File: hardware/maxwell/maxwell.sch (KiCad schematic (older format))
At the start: 33 parts, among them J1 Canbus 1, J10 SPI2_B, J11 BACKUP, J12 UART4, J13 UART5, J14 I2C1, J16 ESP_BM, J17 ESP_PROG, J19 Interconnect (Power), J2 SPI2_C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

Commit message: Updating PWR board to v1.7; adds:
* Fix for footprint of AP9101C (I have the five-pin package; not six)
* Grounding VM on the AP9101C to BAT- to disable current protection;
  I'm using the TPS2113A for current protection, so this feature isn't
  needed.
* Adds I2C-addressable INA219AID current sensor IC.
* Adds I2C-addressable PCF8593 counter for speed measurement.
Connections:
- net labels removed: SPEED
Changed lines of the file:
@@
 Text GLabel 5350 3450 0    60   BiDi ~ 0
 I2C1_SDA
-Text GLabel 5350 3350 0    60   Input ~ 0
-SPEED
-Text GLabel 5350 4500 0    60   Output ~ 0
-SPEED
 Text GLabel 5850 4600 2    60   BiDi ~ 0
 I2C1_SCL

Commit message: Revision 1.9a
* Separates PCB into three boards (from two); adding a new
  'Rectifier' board mounted directly to the 'Power' board via a
  board-to-board connector.
* Switches to active rectification.
* Provide 5V directly to the battery; drop VCC voltage to
  4.3V via a diode drop.
* Adds new WAKE-controlled power switch to reduce quiescent
  current to, essentially, nil, and remove the need
  carefully managing sleep states of various devices.
* Adds 220uF capacitor to 3V3 output on 'Main' PCB.
* Control power to SPI/I2C connector via a new uC-controlled MOSFET.
* Adds clock chip to main uC board for permanent timekeeping and
  alarm-based wakeup.
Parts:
- removed BZ1: Buzzer, coddingtonbear:12mm_buzzer, symbol maxwell-rescue:Buzzer-RESCUE-maxwell
- removed J13: UART5, coddingtonbear:JST_XH_B04B-XH-A_04x2.50mm_Straight_LargePads, symbol maxwell-rescue:Conn_01x04-conn
- removed J14: I2C1, coddingtonbear:JST_XH_B04B-XH-A_04x2.50mm_Straight_LargePads, symbol maxwell-rescue:Conn_01x04-conn
- removed J19: Interconnect (Power), coddingtonbear:IDC-Header_2x08_P2.54mm_Vertical_Largepads, symbol Connector_Generic:Conn_02x08_Odd_Even
- removed Q1: BSS138, coddingtonbear:SOT-23_LargePads, symbol maxwell-rescue:BSS138-RESCUE-maxwell
- removed R4: >35, coddingtonbear:0805_Milling, symbol maxwell-rescue:R-RESCUE-maxwell
- added C30: 0.1u, coddingtonbear:0805_Milling, symbol maxwell-rescue:C-RESCUE-maxwell
- added C31: 220u, coddingtonbear:CP_Tantalum_Case-C_EIA-6032-28_Milling, symbol Device:CP
- added C8, C9: 22p, coddingtonbear:0805_Milling, symbol maxwell-rescue:C-RESCUE-maxwell
- added D2: MBR1020VL, coddingtonbear:D_SOD-123_LargePads, symbol Device:D_Schottky
- added J15: I2C1, coddingtonbear:JST_XH_B04B-XH-A_04x2.50mm_Straight_LargePads, symbol maxwell-rescue:Conn_01x04-conn
- added Q1, Q2: DMG2302UK, coddingtonbear:SOT-23_LargePads, symbol Device:Q_NMOS_GSD
- added R32, R34, R35: 10k, coddingtonbear:0805_Milling, symbol maxwell-rescue:R-RESCUE-maxwell
- added SW1: SW_Push, coddingtonbear:SMD_MINI_BLACK_TACTILE_SWITCH, symbol Switch:SW_Push
- added U9: MCP79411-I/SN, coddingtonbear:SOIC-8_3.9x4.9mm_P1.27mm_LargePads, symbol Timer:MCP7940N-xSN
- added Y1: 32.768k, Crystal:Crystal_SMD_SeikoEpson_MC306-4Pin_8.0x3.2mm_HandSoldering, symbol maxwell-rescue:Crystal_GND23_Small-device
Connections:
- net labels added: +3V3_B, ENABLE_AUX, ENABLE_LEDS, GNDAUX, GND_B, I2C1_SCL_B, I2C1_SDA_B, VCC_B, WAKE_B, WAKE_B_SIG
- net labels removed: +3V3, BUZZER, CAN_DISABLE, GND, GNDPWR, I2C1_SCL, I2C1_SDA, POWER_ON, UART5_RX, UART5_TX, VCC
- wire segments 131 -> 168
- no-connect marks 26 -> 28
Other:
- moved on the sheet: C4, C5, J1, J10, J11, J12, J2, J20, J3, J5, R1, R31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

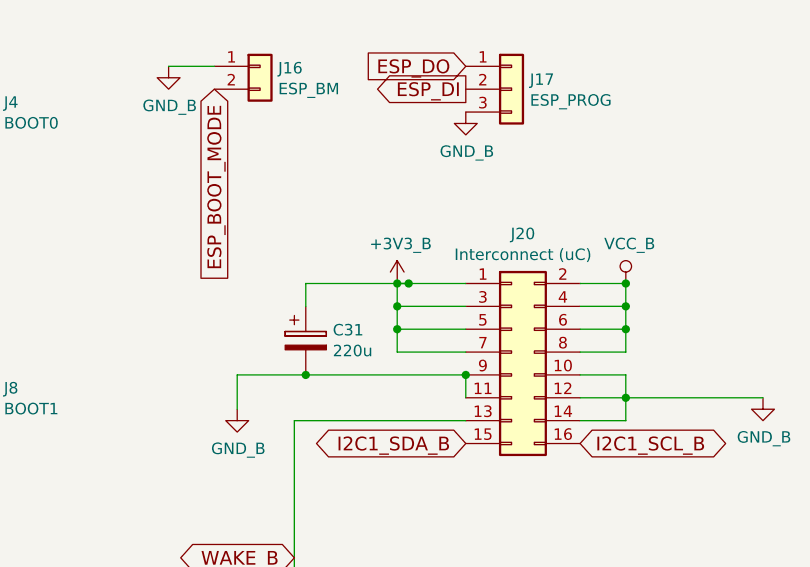
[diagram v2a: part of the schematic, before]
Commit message: Missing connection from diode controller to VDYN+; bodged.
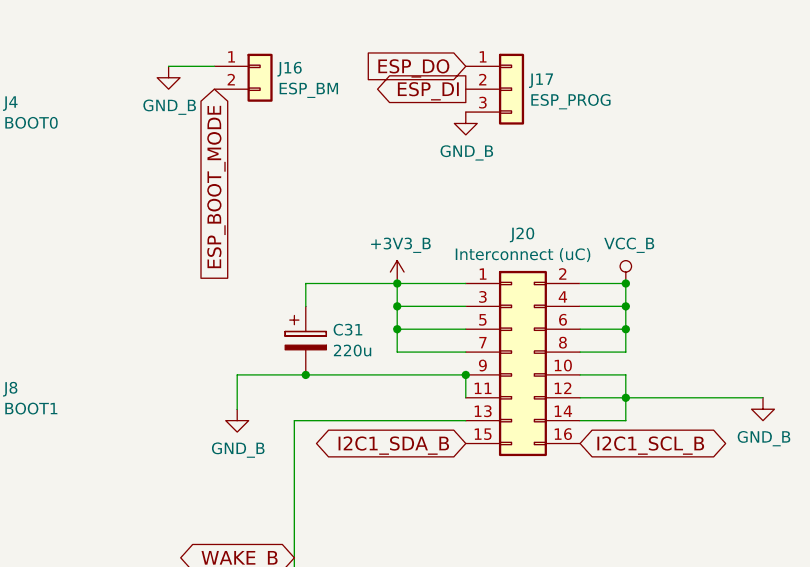
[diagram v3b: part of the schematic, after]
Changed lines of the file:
@@
 Wire Wire Line
 	4650 1900 5050 1900
-Connection ~ 5100 1900
-Wire Wire Line
-	5100 1900 5050 1900
 Wire Wire Line
 	4350 6150 5300 6150
-Wire Wire Line
-	5050 1900 5350 1900
 Connection ~ 5300 6150
 Wire Wire Line
 	5300 6150 5300 6400
+Wire Wire Line
+	5050 1900 5350 1900
 $EndSCHEMATC

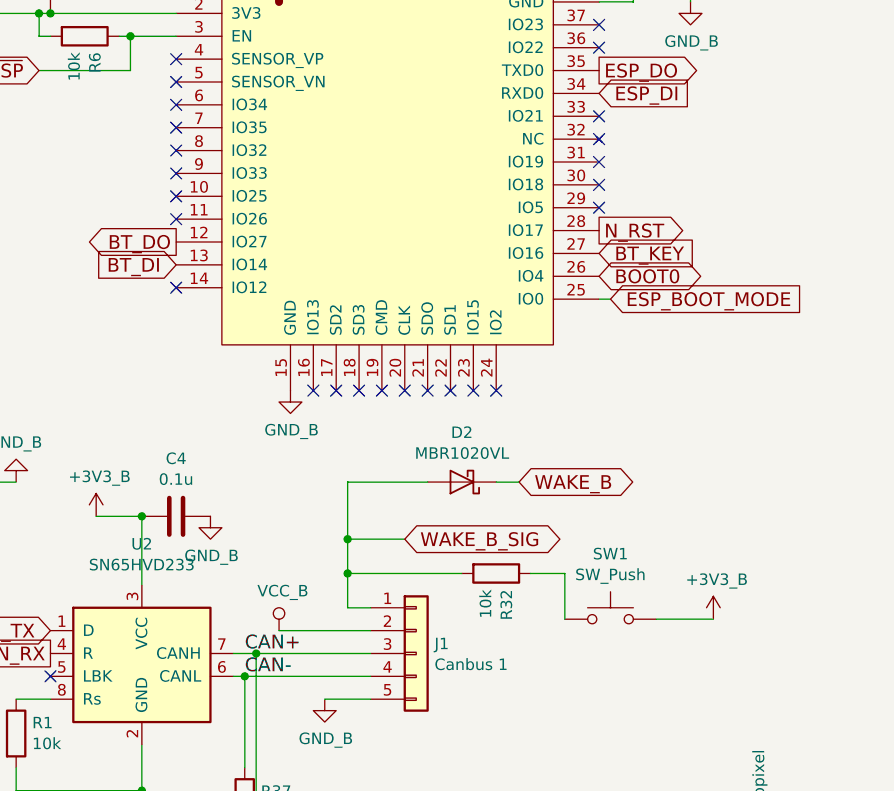
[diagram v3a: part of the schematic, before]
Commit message: Fixing errata:
* Connecting ESP32 to WAKE to ensure that the ESP32 can keep
  the power on while doing things like flashing the uC.
* Pull power button high to VCC via a diode instead of
  3V3 which is the very thing the power button will be
  turning on.
* Updating sense resistor to 100mOhm instead of 20mOhm.
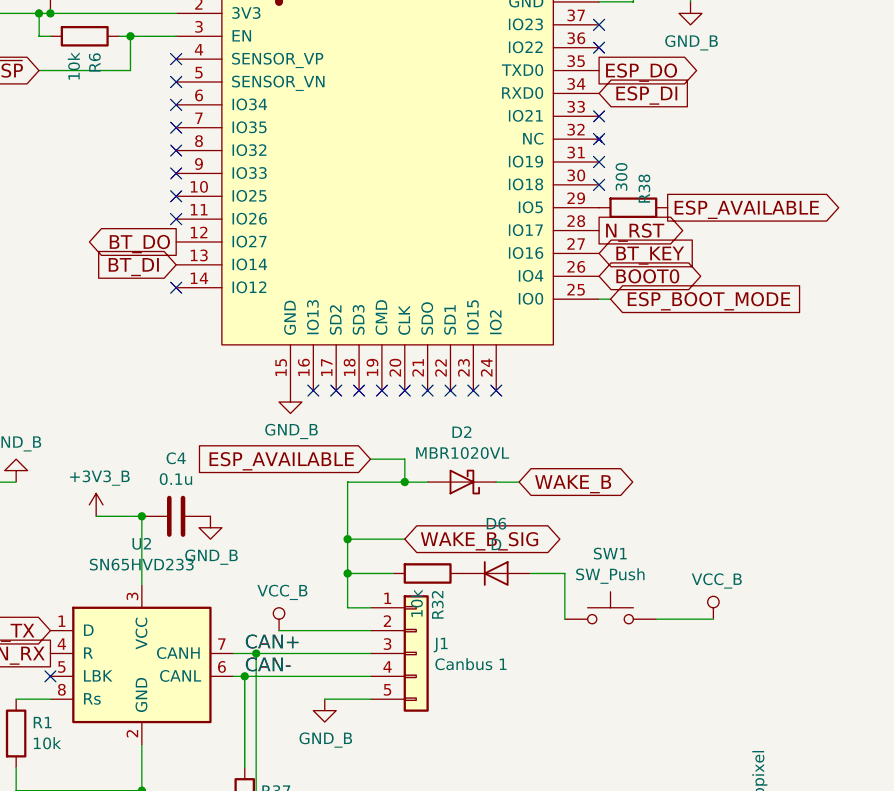
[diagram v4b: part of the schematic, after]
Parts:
- added D6: D, Diode_SMD:D_SOD-323_HandSoldering, symbol Device:D
- added R38: 300, coddingtonbear:0805_Milling, symbol maxwell-rescue:R-RESCUE-maxwell
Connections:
- net +3V3_B: no longer SW1.2
- net VCC_B: now also SW1.2
- net at U5.29 (IO5): now also R38.2
- net at R32.1: now also D6.1 (K); no longer SW1.1
- net WAKE_B_SIG renamed ESP_AVAILABLE
- net ESP_AVAILABLE: now also R38.1
- new net: D6.2 (A), SW1.1
- no-connect marks 28 -> 27
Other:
- moved on the sheet: R32
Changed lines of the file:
@@
 NoConn ~ 10000 2350
 NoConn ~ 10000 2450
-NoConn ~ 10000 2550
 NoConn ~ 8750 3350
 NoConn ~ 8850 3350
@@
 	9550 3750 9650 3750
 Wire Wire Line
-	9250 3750 8900 3750
+	9250 3750 9150 3750
 Wire Wire Line
 	8900 3750 8900 4000
@@
 	1    0    0    -1
 $EndComp
-$Comp
-L coddingtonbear:+3V3_B #PWR0190
-U 1 1 5CC42E7E
-P 10500 4350
-F 0 "#PWR0190" H 10500 4200 50  0001 C CNN
-F 1 "+3V3_B" H 10515 4523 50  0000 C CNN
-F 2 "" H 10500 4350 50  0001 C CNN
-F 3 "" H 10500 4350 50  0001 C CNN
-	1    10500 4350
-	1    0    0    -1
-$EndComp
 Wire Wire Line
 	10500 4350 10250 4350
-Wire Wire Line
-	8900 4000 8900 4150
 $Comp
 L maxwell-rescue:R-RESCUE-maxwell R32
 U 1 1 5CC502FE
-P 9550 4150
-F 0 "R32" H 9620 4196 50  0000 L CNN
-F 1 "10k" H 9620 4105 50  0000 L CNN
-F 2 "coddingtonbear:0805_Milling" V 9480 4150 50  0001 C CNN
-F 3 "" H 9550 4150 50  0001 C CNN
-	1    9550 4150
+P 9250 4150
+F 0 "R32" H 9320 4196 50  0000 L CNN
+F 1 "10k" H 9320 4105 50  0000 L CNN
+F 2 "coddingtonbear:0805_Milling" V 9180 4150 50  0001 C CNN
+F 3 "" H 9250 4150 50  0001 C CNN
+	1    9250 4150
 	0    1    1    0
 $EndComp
-Wire Wire Line
-	9400 4150 8900 4150
-Connection ~ 8900 4150
-Wire Wire Line
-	8900 4150 8900 4300
-Wire Wire Line
-	9700 4150 9850 4150
 Wire Wire Line
 	9850 4150 9850 4350
@@
 Wire Wire Line
 	5050 1900 5350 1900
+$Comp
+L coddingtonbear:VCC_B #PWR0190
+U 1 1 5C70A807
+P 10500 4350
+F 0 "#PWR0190" H 10500 4200 50  0001 C CNN
+F 1 "VCC_B" H 10517 4523 50  0000 C CNN
+F 2 "" H 10500 4350 50  0001 C CNN
+F 3 "" H 10500 4350 50  0001 C CNN
+	1    10500 4350
+	1    0    0    -1
+$EndComp
+Wire Wire Line
+	8900 4000 8900 4150
+$Comp
+L Device:D D6
+U 1 1 5C70AC6C
+P 9550 4150
+F 0 "D6" H 9550 4366 50  0000 C CNN
+F 1 "D" H 9550 4275 50  0000 C CNN
+F 2 "Diode_SMD:D_SOD-323_HandSoldering" H 9550 4150 50  0001 C CNN
+F 3 "~" H 9550 4150 50  0001 C CNN
+	1    9550 4150
+	1    0    0    -1
+$EndComp
+Wire Wire Line
+	9850 4150 9700 4150
+Wire Wire Line
+	9100 4150 8900 4150
+Connection ~ 8900 4150
+Wire Wire Line
+	8900 4150 8900 4300
+Text GLabel 10300 2550 2    60   Output ~ 0
+ESP_AVAILABLE
+$Comp
+L maxwell-rescue:R-RESCUE-maxwell R38
+U 1 1 5C71B19B
+P 10150 2550
+F 0 "R38" H 10000 2600 50  0000 L CNN
+F 1 "300" H 9950 2500 50  0000 L CNN
+F 2 "coddingtonbear:0805_Milling" V 10080 2550 50  0001 C CNN
+F 3 "" H 10150 2550 50  0001 C CNN
+	1    10150 2550
+	0    1    1    0
+$EndComp
+Text GLabel 9000 3650 0    60   Input ~ 0
+ESP_AVAILABLE
+Wire Wire Line
+	9000 3650 9150 3650
+Wire Wire Line
+	9150 3650 9150 3750
+Connection ~ 9150 3750
+Wire Wire Line
+	9150 3750 8900 3750
 $EndSCHEMATC

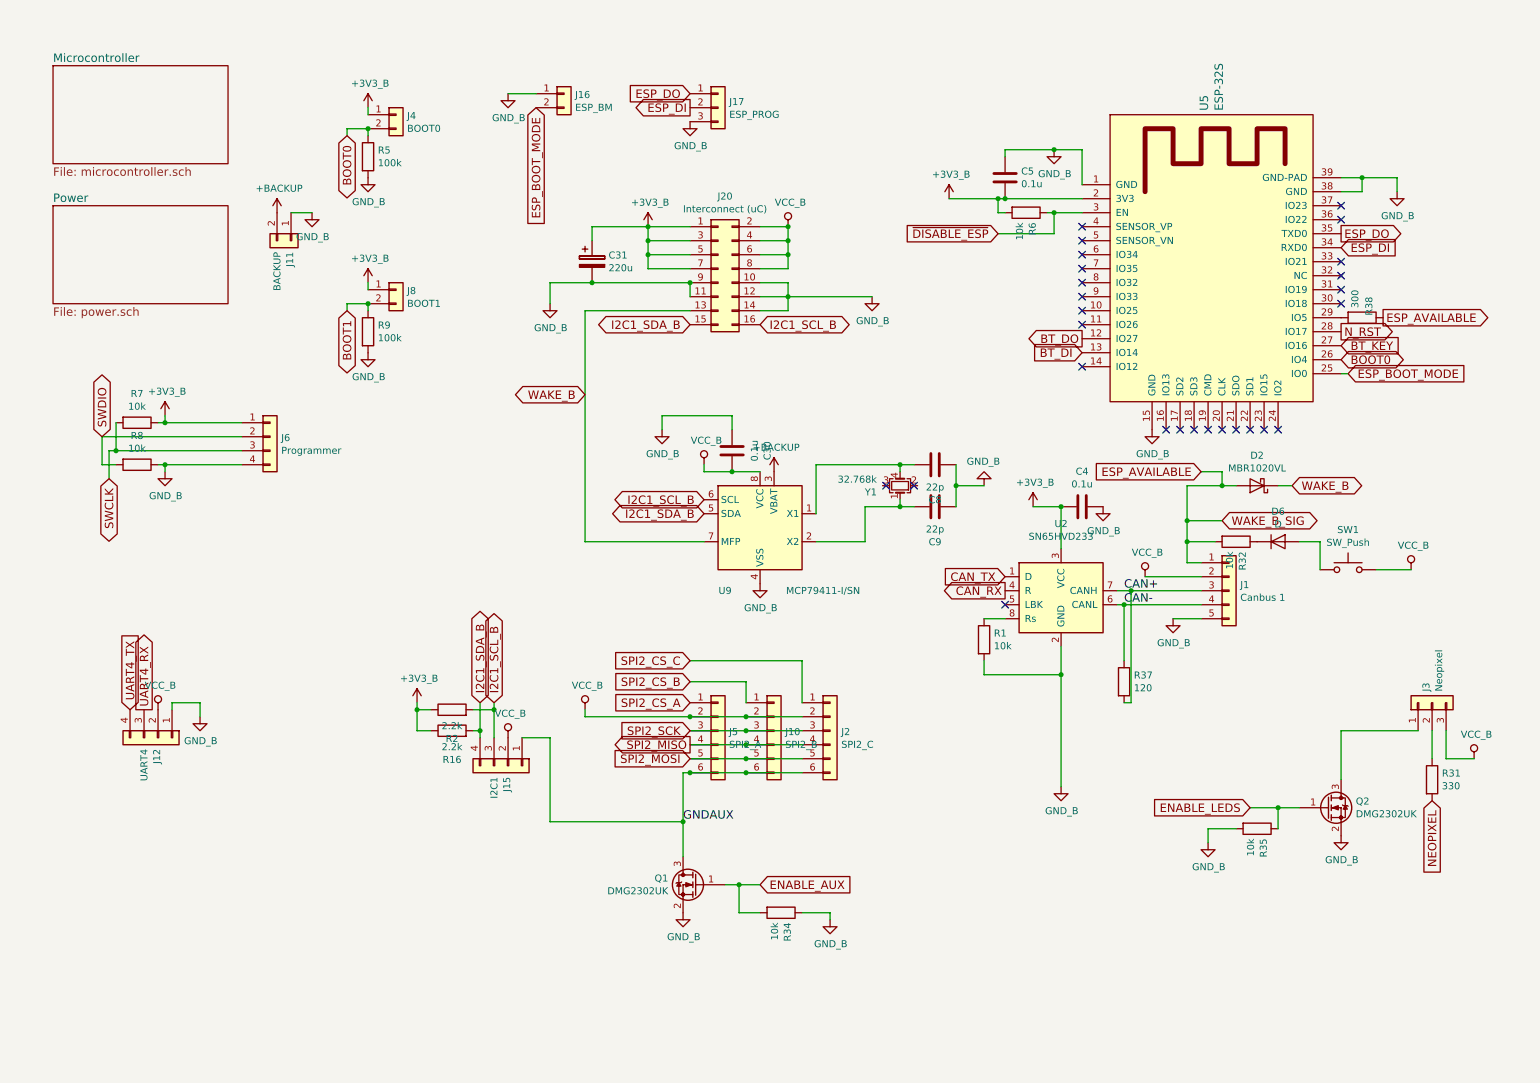
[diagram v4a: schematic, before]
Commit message: Maxwell v1.9.1
While sciencing earlier today, I narrowed down my surprisingly-high
quiescent current problem to being how I've handled switching
off the Neopixels and SPI-connected devices.  Historicaly,
those were switched using a low-side N-Channel MOSFET. With these
changes, these will be switched via a high-side P-Channel MOSFET
(itself controlled by an N-Channel MOSFET to ensure that the
microcontroller isn't exposed to VCC).

* Swaps Neopixel power-off device from low-side N-Channel MOSFET
  to P-Channel MOSFET controlled by an N-Channel MOSFET.
* Swaps SPI power-off device from low-side N-Channel MOSFET
  to P-Channel MOSFET controlled by an N-Channel MOSFET.
* Fixes a few erroneous resistor values.
* Adds a diode between RTC and WAKE to prevent RTC from being
  able to turn off the power, only turn it on.

* Switches off
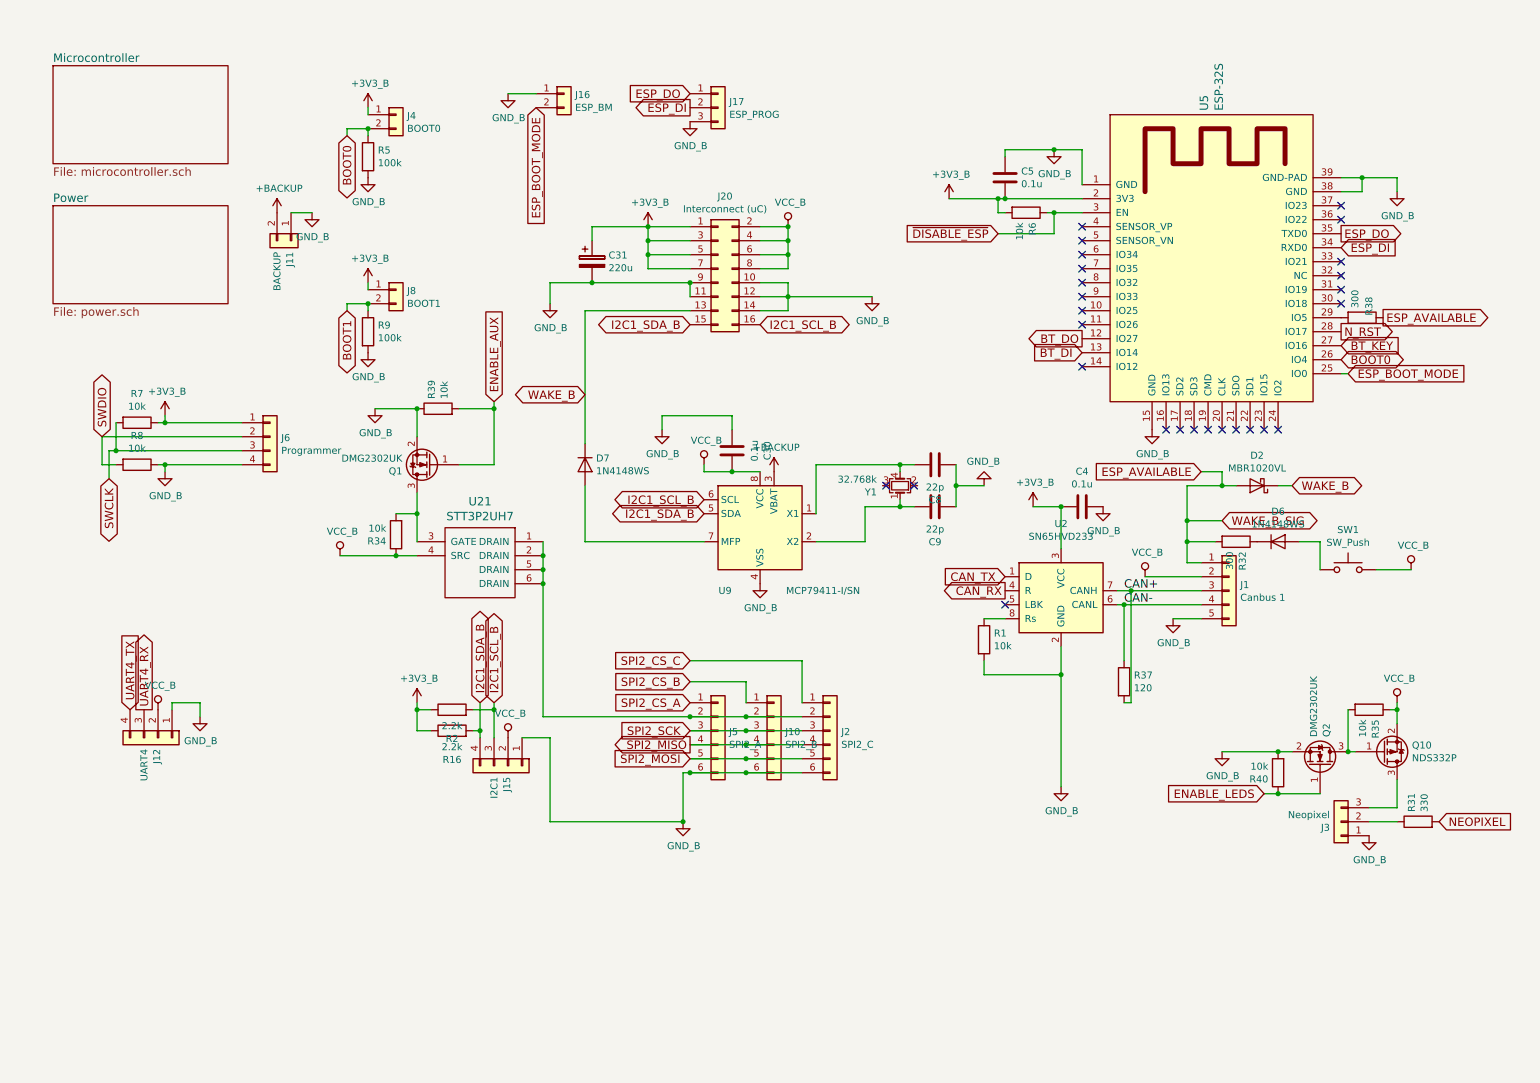
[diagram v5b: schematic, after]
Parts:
- added D7: 1N4148WS, Diode_SMD:D_SOD-323_HandSoldering, symbol Device:D
- added Q10: NDS332P, coddingtonbear:SOT-23_LargePads, symbol Device:Q_PMOS_GSD
- added R39, R40: 10k, coddingtonbear:0805_Milling, symbol maxwell-rescue:R-RESCUE-maxwell
- added U21: STT3P2UH7, Package_TO_SOT_SMD:SOT-23-6_Handsoldering, symbol coddingtonbear:STT3P2UH7
- D6: value D -> 1N4148WS
- R32: value 10k -> 300
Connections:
- net ENABLE_AUX: now also R39.2; no longer R34.2
- net ENABLE_LEDS: now also R40.1; no longer R35.1
- net GND_B: now also J10.6 (Pin_6), J15.1 (Pin_1), J2.6 (Pin_6), J3.1 (Pin_1), J5.6 (Pin_6), R39.1, R40.2; no longer R34.1, R35.2
- net VCC_B: now also R34.1, R35.1, Q10.2 (S), U21.4 (SRC); no longer J10.2 (Pin_2), J2.2 (Pin_2), J3.3 (Pin_3), J5.2 (Pin_2)
- net WAKE_B: now also D7.1 (K); no longer U9.7 (MFP)
- net at Q2.3 (D): now also R35.2, Q10.1 (G); no longer J3.1 (Pin_1)
- removed net GNDAUX: J10.6 (Pin_6), J15.1 (Pin_1), J2.6 (Pin_6), J5.6 (Pin_6), Q1.3 (D)
- new net: J3.3 (Pin_3), Q10.3 (D)
- new net: J10.2 (Pin_2), J2.2 (Pin_2), J5.2 (Pin_2), U21.1 (DRAIN), U21.2 (DRAIN), U21.5 (DRAIN), U21.6 (DRAIN)
- new net: D7.2 (A), U9.7 (MFP)
- new net: Q1.3 (D), R34.2, U21.3 (GATE)
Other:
- moved on the sheet: J3, Q2, R31, R34, R35
